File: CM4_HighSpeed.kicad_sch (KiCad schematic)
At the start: 11 parts, among them J15 Conn_01x22_Female, J4 DF40C-24DP-0.4V_51_, J5 DF40C-24DP-0.4V_51_, J6 THD-02-R, J8 HDMI_D_1.4, U12 RT9742SNGV

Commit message: library management
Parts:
- J4, J5: footprint DF40C24DP04V51 -> Open-HD:DF40C24DP04V51
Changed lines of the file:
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@@
     (property "Reference" "J4" (id 0) (at 174.625 95.25 0))
     (property "Value" "DF40C-24DP-0.4V_51_" (id 1) (at 174.625 97.79 0))
-    (property "Footprint" "DF40C24DP04V51" (id 2) (at 182.88 100.965 0)
+    (property "Footprint" "Open-HD:DF40C24DP04V51" (id 2) (at 182.88 100.965 0)
       (effects (font (size 1.27 1.27)) (justify left) hide)
     )
@@
     (property "Reference" "J5" (id 0) (at 175.26 32.385 0))
     (property "Value" "DF40C-24DP-0.4V_51_" (id 1) (at 175.26 34.925 0))
-    (property "Footprint" "DF40C24DP04V51" (id 2) (at 183.515 38.1 0)
+    (property "Footprint" "Open-HD:DF40C24DP04V51" (id 2) (at 183.515 38.1 0)
       (effects (font (size 1.27 1.27)) (justify left) hide)
     )

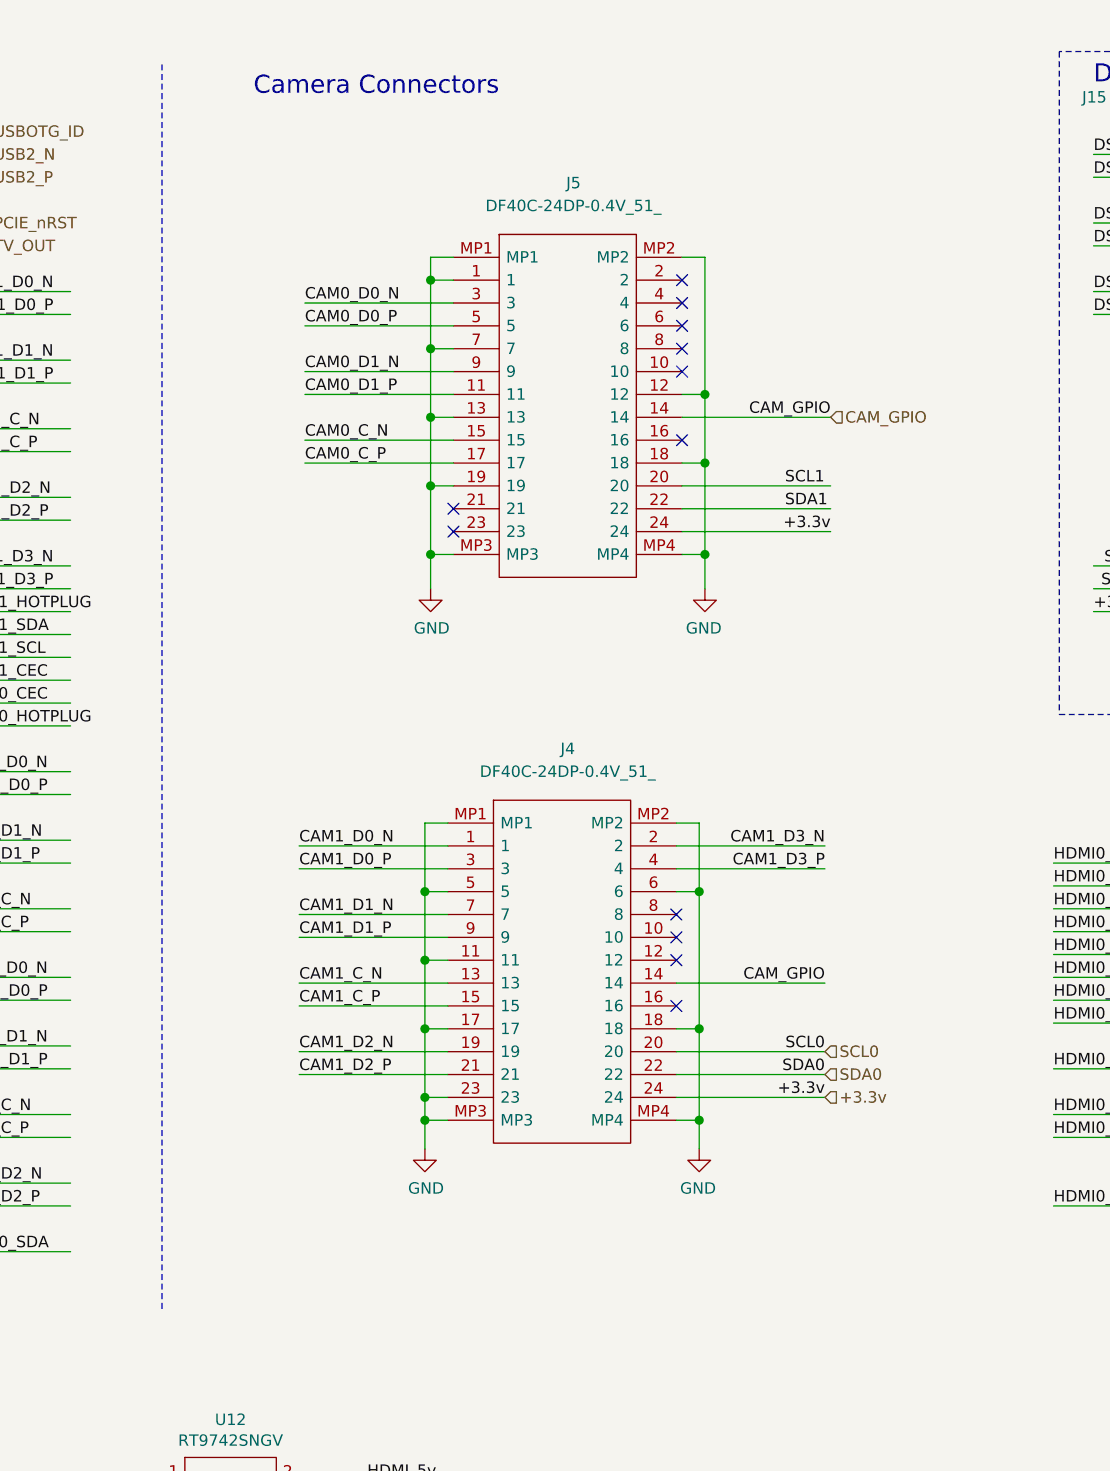
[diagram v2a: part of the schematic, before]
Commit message: starting to lay out switching regulator
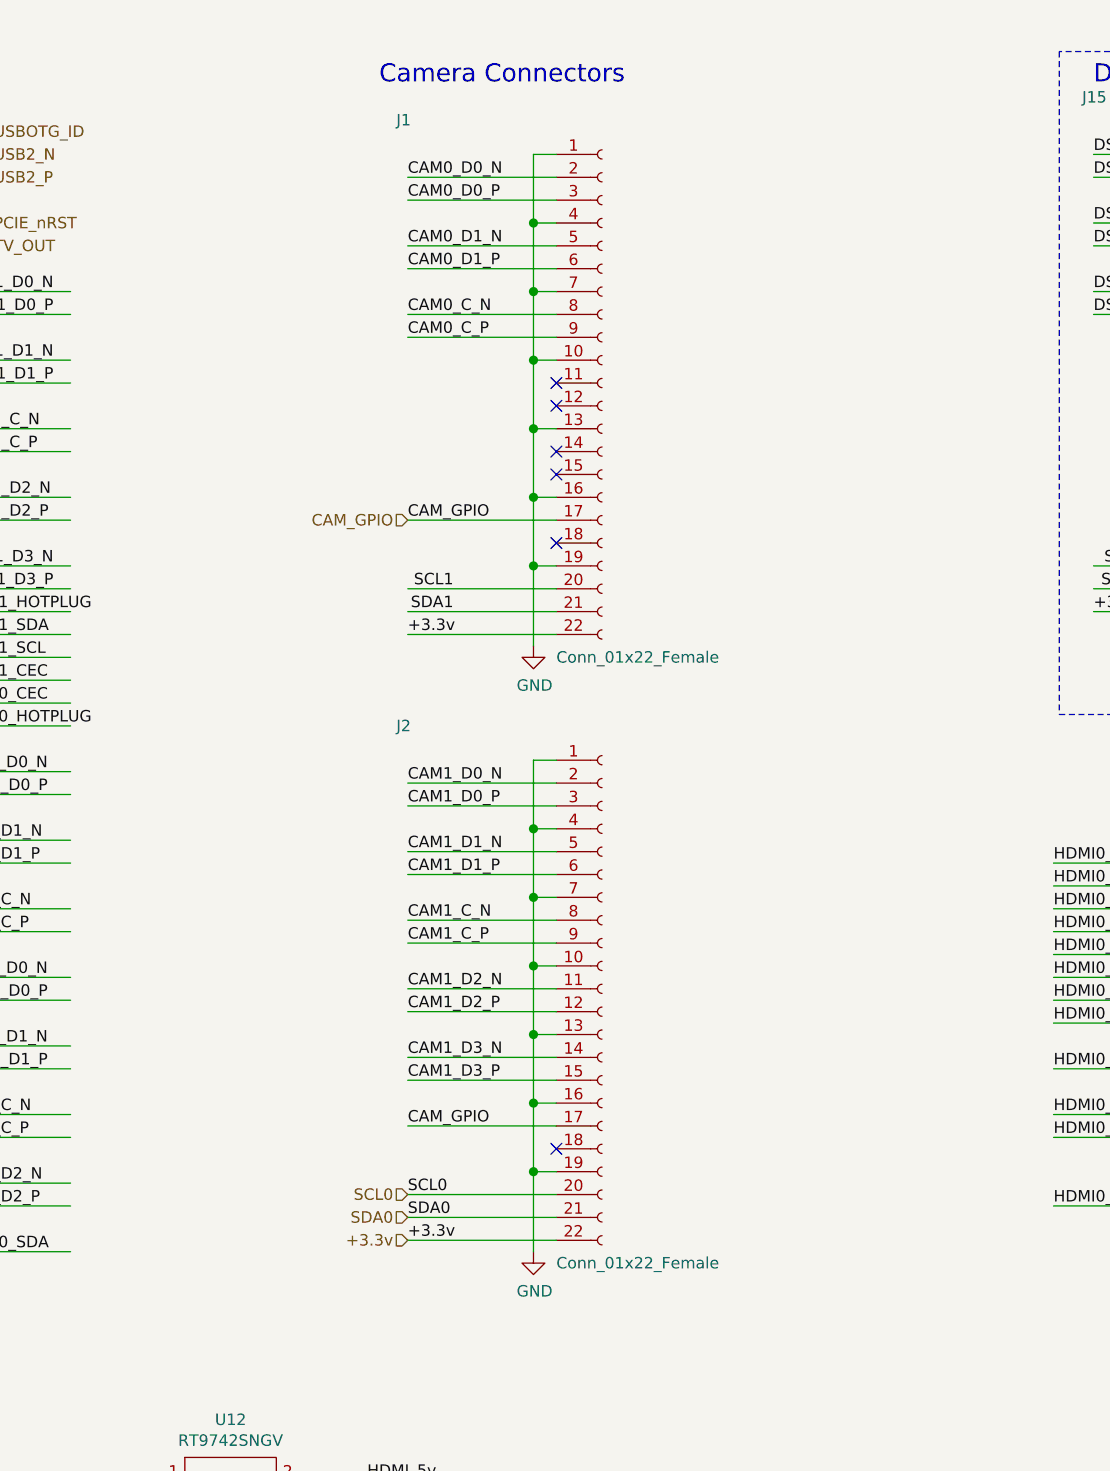
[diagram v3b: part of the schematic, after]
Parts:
- removed J4, J5: DF40C-24DP-0.4V_51_, Open-HD:DF40C24DP04V51, symbol DF40C-24DP-0.4V_51_:DF40C-24DP-0.4V_51_
- added J1, J2: Conn_01x22_Female, Connector_FFC-FPC:Hirose_FH12-22S-0.5SH_1x22-1MP_P0.50mm_Horizontal, symbol Connector:Conn_01x22_Female
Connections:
- net +3.3v: now also J1.22 (Pin_22), J2.22 (Pin_22)
- net CAM0_C_N: now also J1.8 (Pin_8)
- net CAM0_C_P: now also J1.9 (Pin_9)
- net CAM0_D0_N: now also J1.2 (Pin_2)
- net CAM0_D0_P: now also J1.3 (Pin_3)
- net CAM0_D1_N: now also J1.5 (Pin_5)
- net CAM0_D1_P: now also J1.6 (Pin_6)
- net CAM1_C_N: now also J2.8 (Pin_8)
- net CAM1_C_P: now also J2.9 (Pin_9)
- net CAM1_D0_N: now also J2.2 (Pin_2)
- net CAM1_D0_P: now also J2.3 (Pin_3)
- net CAM1_D1_N: now also J2.5 (Pin_5)
- net CAM1_D1_P: now also J2.6 (Pin_6)
- net CAM1_D2_N: now also J2.11 (Pin_11)
- net CAM1_D2_P: now also J2.12 (Pin_12)
- net CAM1_D3_N: now also J2.14 (Pin_14)
- net CAM1_D3_P: now also J2.15 (Pin_15)
- net CAM_GPIO: now also J1.17 (Pin_17), J2.17 (Pin_17)
- net GND: now also J1.1 (Pin_1), J1.10 (Pin_10), J1.13 (Pin_13), J1.16 (Pin_16), J1.19 (Pin_19), J1.4 (Pin_4), J1.7 (Pin_7), J2.1 (Pin_1), J2.10 (Pin_10), J2.13 (Pin_13), J2.16 (Pin_16), J2.19 (Pin_19), J2.4 (Pin_4), J2.7 (Pin_7)
- net SCL0: now also J2.20 (Pin_20)
- net SCL1: now also J1.20 (Pin_20)
- net SDA0: now also J2.21 (Pin_21)
- net SDA1: now also J1.21 (Pin_21)
- no-connect marks 21 -> 15

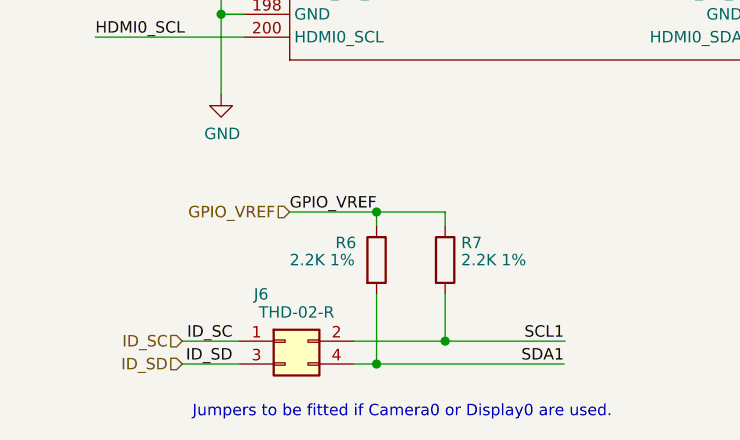
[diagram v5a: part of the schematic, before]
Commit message: lots of changes, added usb power connections, gpio, hdmi, etc
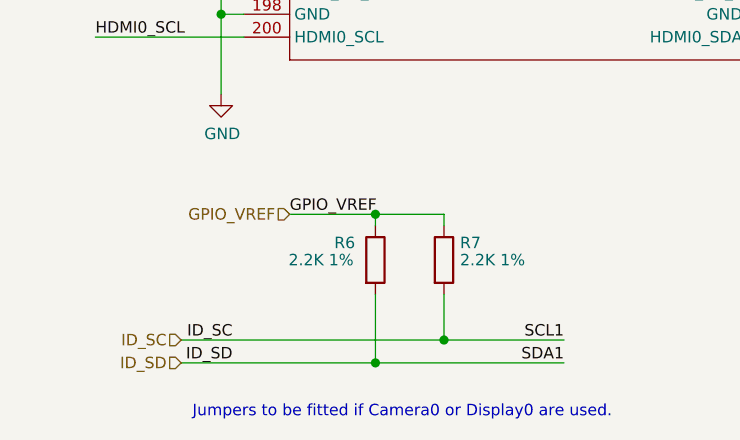
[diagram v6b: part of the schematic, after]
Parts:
- removed J6: THD-02-R, Connector_PinHeader_2.54mm:PinHeader_2x02_P2.54mm_Vertical, symbol Connector_Generic:Conn_02x02_Odd_Even
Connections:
- net SCL1 is gone; now on net ID_SC: J1.20 (Pin_20), J15.20 (Pin_20), R7.2
- net SDA1 is gone; now on net ID_SD: J1.21 (Pin_21), J15.21 (Pin_21), R6.2

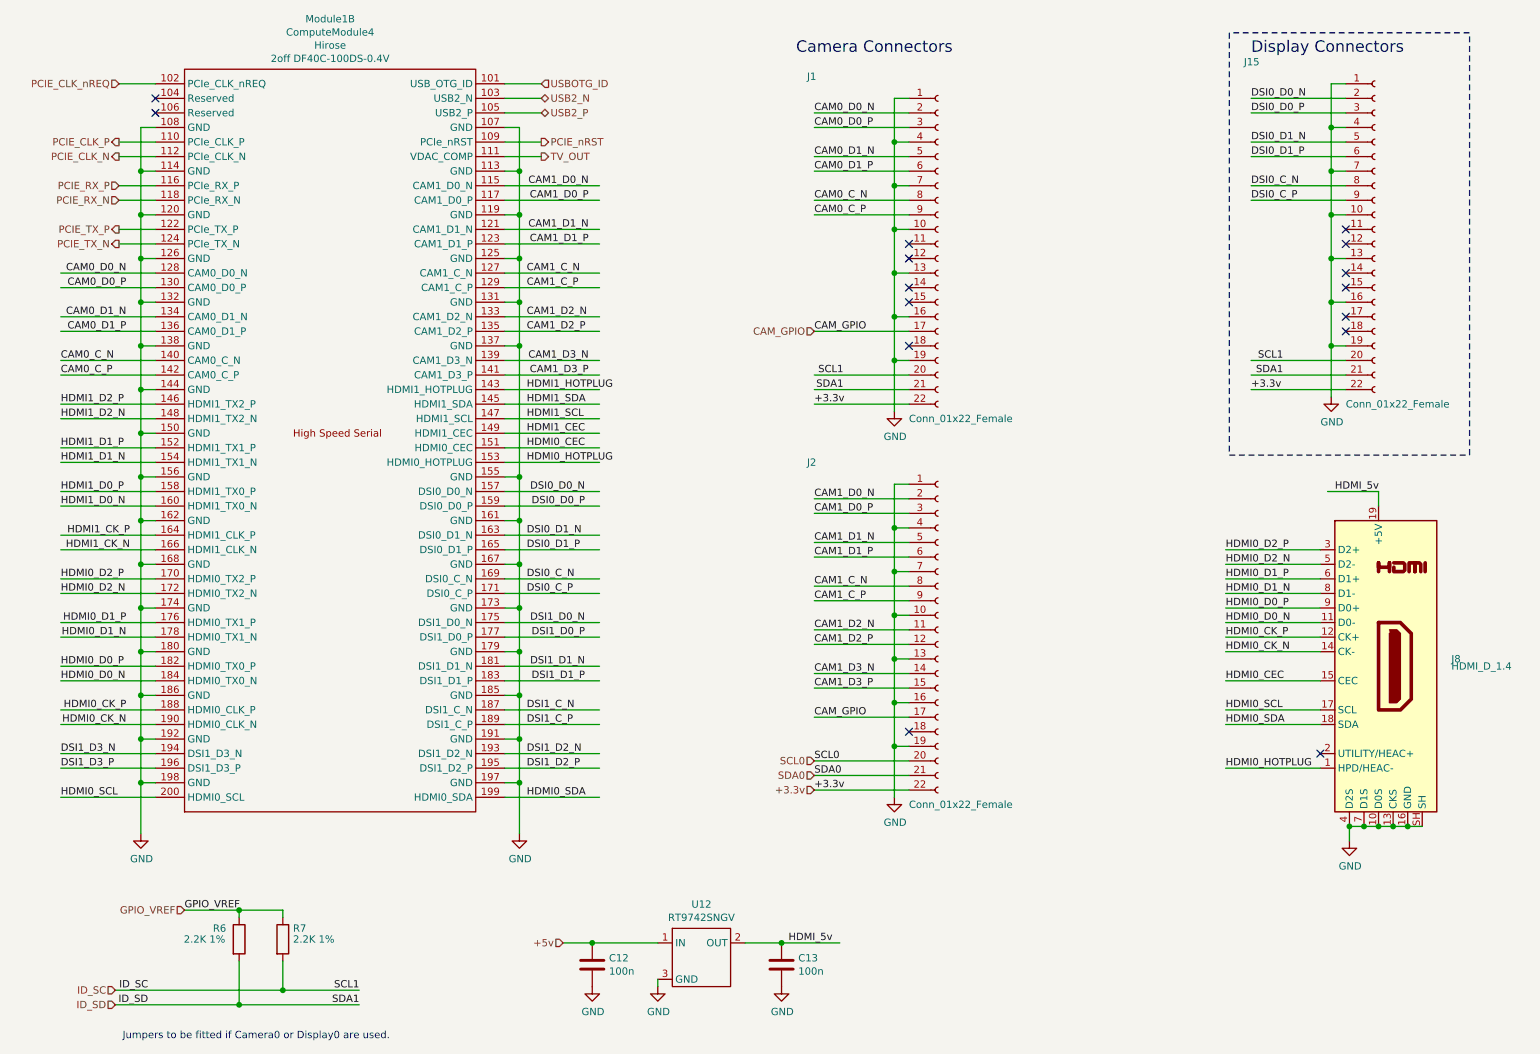
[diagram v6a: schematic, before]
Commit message: Changed footprint to match CM4, removed Ethernet and HDMI
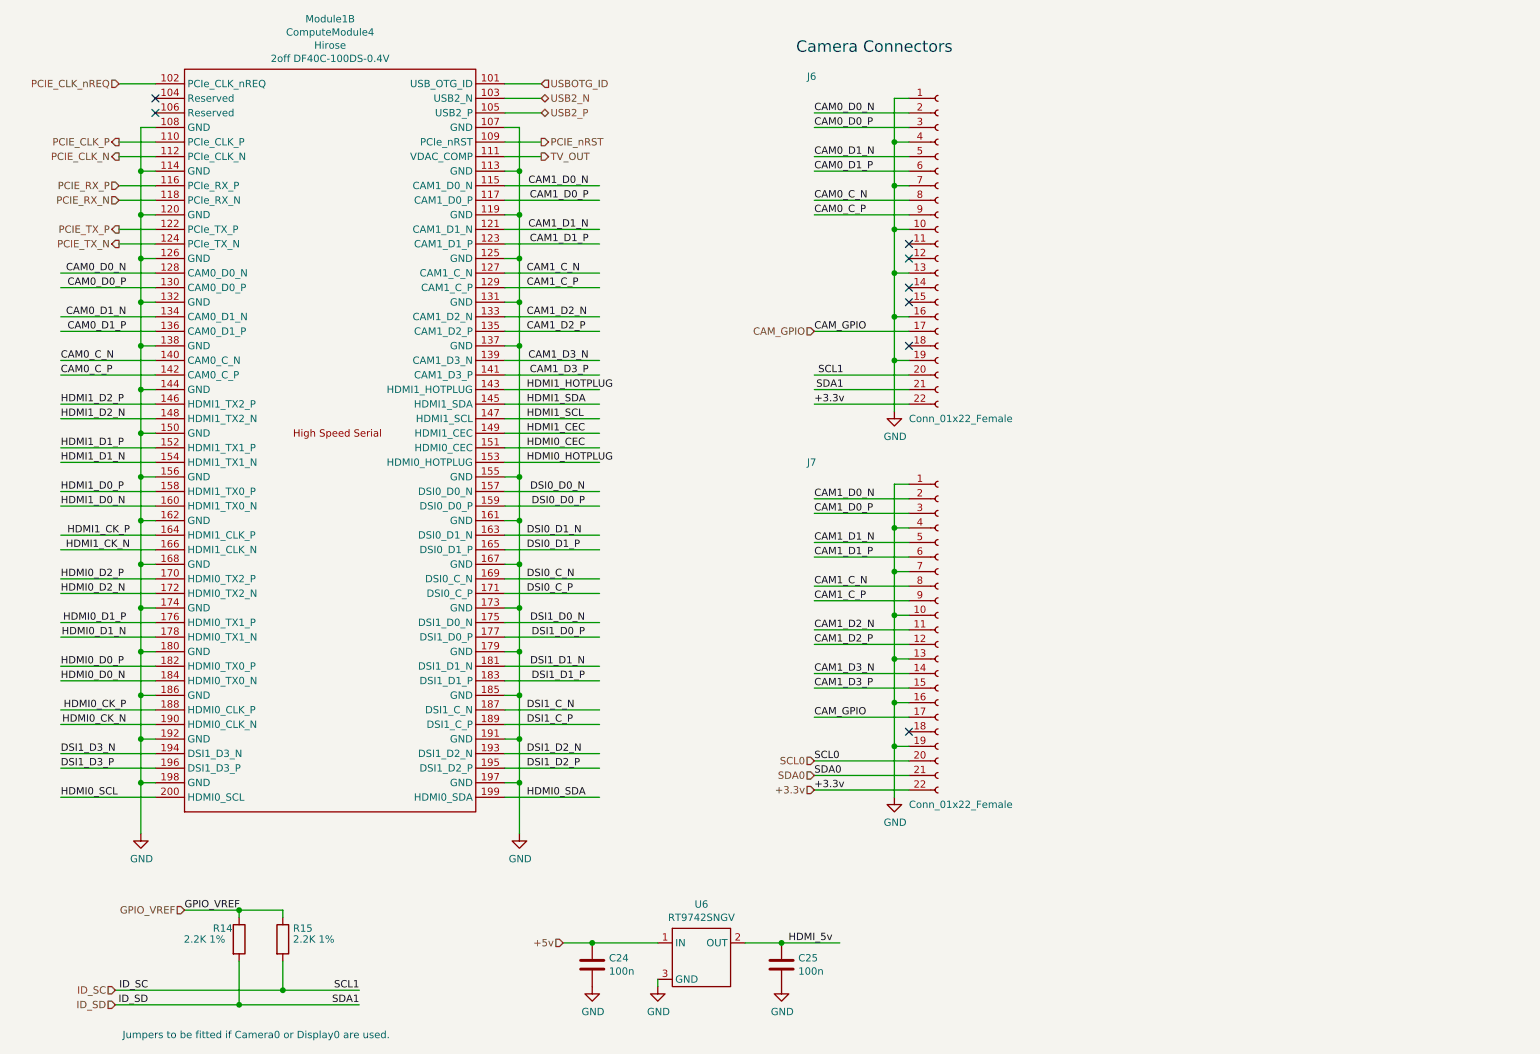
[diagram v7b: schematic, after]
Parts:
- removed J15: Conn_01x22_Female, Connector_FFC-FPC:Hirose_FH12-22S-0.5SH_1x22-1MP_P0.50mm_Horizontal, symbol Connector:Conn_01x22_Female
- removed J8: HDMI_D_1.4, Connector_HDMI:HDMI_Micro-D_Molex_46765-0x01, symbol Connector:HDMI_D_1.4
- renumbered C12 to C24, C13 to C25, J1 to J6, J2 to J7, R6 to R14, R7 to R15, U12 to U6
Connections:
- no-connect marks 15 -> 8
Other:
- note removed: "Display Connectors"
